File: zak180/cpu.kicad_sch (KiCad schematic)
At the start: 19 parts, among them IC1 Z8-L180-S180-180-PLCC-68, U16 74HC08, U20 74HC688, U21 74HC688, U23 74HC74, U24 74HC02, U8 74HC138, Y2 16 MHz

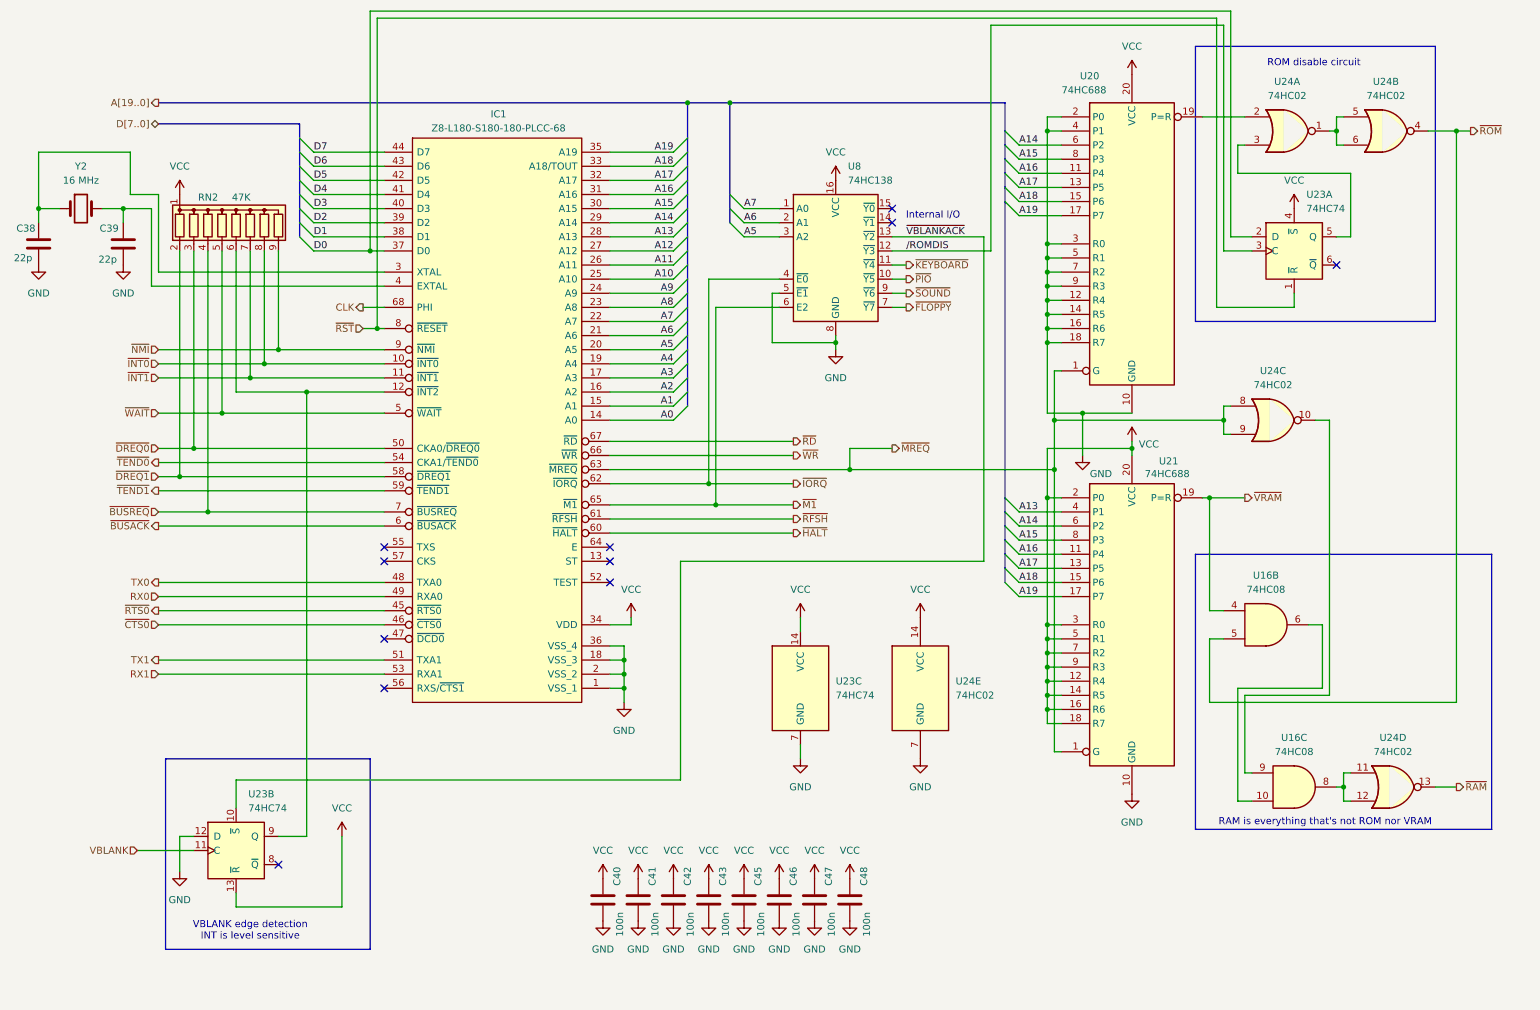
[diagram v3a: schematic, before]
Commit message: HW: Change RAM to static
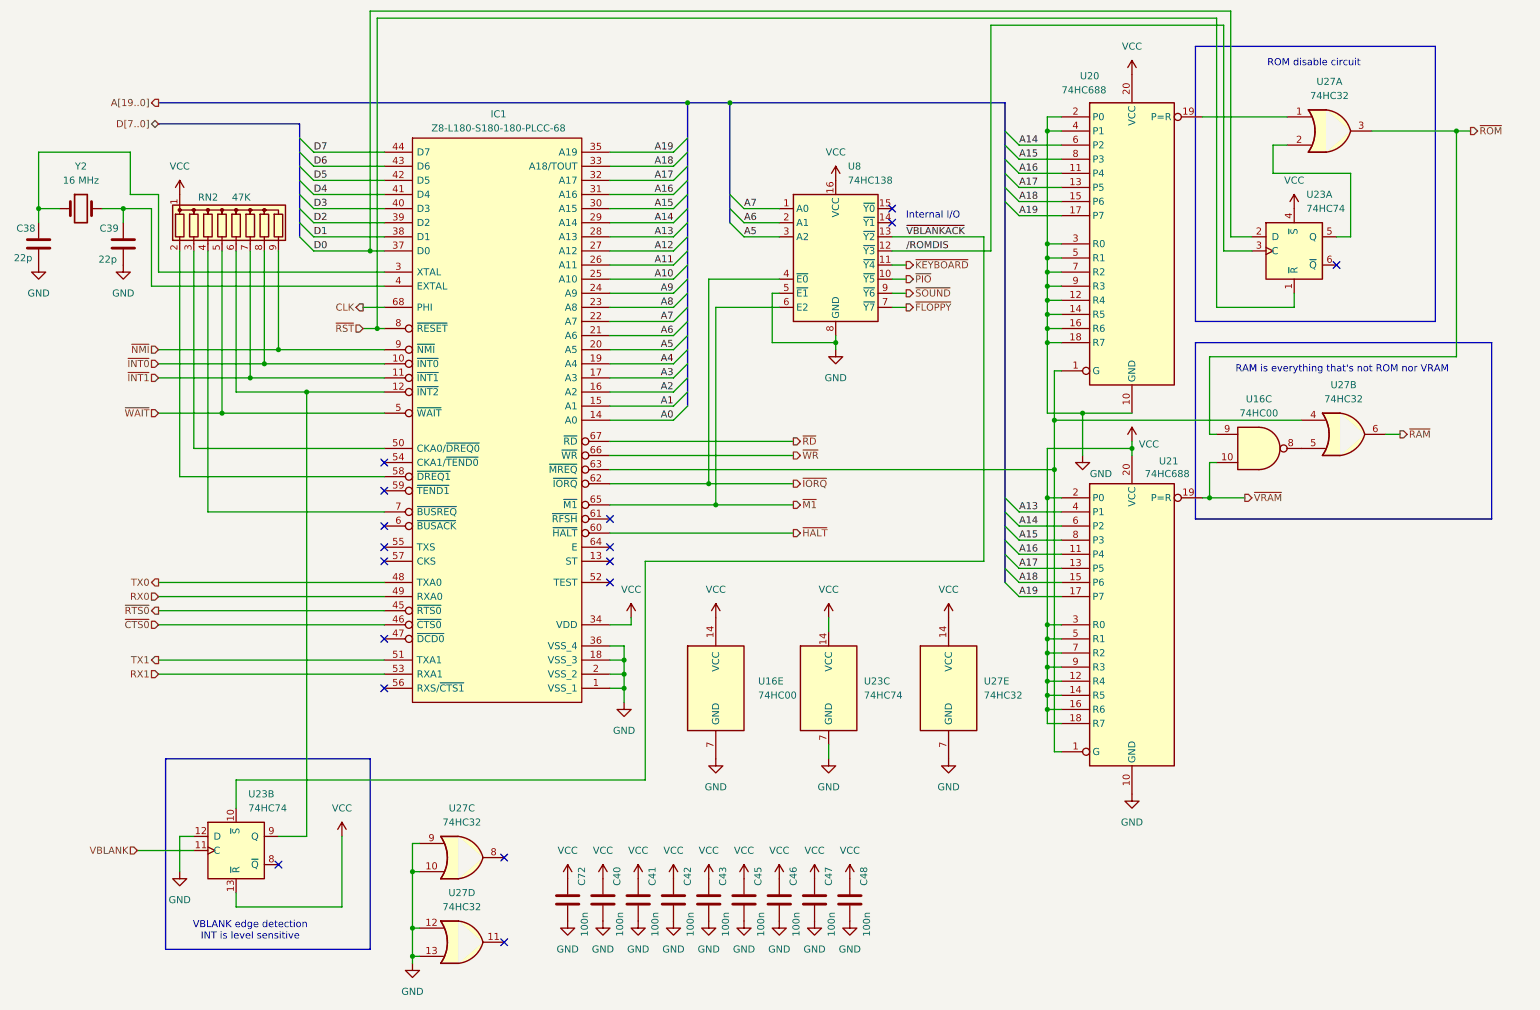
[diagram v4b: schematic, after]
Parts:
- removed U16: 74HC08, Package_DIP:DIP-14_W7.62mm, symbol 74xx:74LS08
- removed U24: 74HC02, symbol 74xx:74HC02
- added C72: 100n, Capacitor_THT:C_Disc_D5.0mm_W2.5mm_P2.50mm, symbol Device:C
- added U16: 74HC00, Package_DIP:DIP-14_W7.62mm, symbol 74xx:74HC00
- added U27: 74HC32, Package_DIP:DIP-14_W7.62mm, symbol 74xx:74LS32
- U20, U21: footprint (none) -> Package_DIP:DIP-20_W7.62mm
- U23: footprint (none) -> Package_DIP:DIP-14_W7.62mm
- U8: footprint (none) -> Package_DIP:DIP-16_W7.62mm
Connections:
- net GND: now also C72.2, U16.7 (GND), U27.10, U27.12, U27.13, U27.7 (GND), U27.9
- net VCC: now also C72.1, U16.14 (VCC), U27.14 (VCC)
- net ~{RAM}: now also U27.6
- net ~{ROM}: now also U16.9, U27.3
- net ~{VRAM}: now also U16.10
- net at U23.5 (Q): now also U27.2
- net at U20.19 (P=R): now also U27.1
- net ~{BUSACK}: no longer names the net of IC1.6 (~{BUSACK})
- net ~{BUSREQ}: no longer names the net of IC1.7 (~{BUSREQ}), RN2.4 (R3)
- net ~{DREQ0}: no longer names the net of IC1.50 (CKA0/~{DREQ0}), RN2.3 (R2)
- net ~{DREQ1}: no longer names the net of IC1.58 (~{DREQ1}), RN2.2 (R1)
- net ~{MREQ}: no longer names the net of IC1.63 (~{MREQ}), U20.1 (G), U21.1 (G)
- net ~{MREQ}: now also U27.4
- net ~{RFSH}: no longer names the net of IC1.61 (~{RFSH})
- net ~{TEND0}: no longer names the net of IC1.54 (CKA1/~{TEND0})
- net ~{TEND1}: no longer names the net of IC1.59 (~{TEND1})
- new net: U16.8, U27.5
- no-connect marks 11 -> 17
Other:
- moved on the sheet: U23C
